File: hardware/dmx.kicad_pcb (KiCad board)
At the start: 4 copper layers, 70 x 70 mm, 63 parts, among them J101 CORTEX-DEBUG, J102 JAE_DX07S016JA3, J201 SJ2-25404B-SMT-TR, J301 SJ2-25404B-SMT-TR, SW101 SW_Push, SW102 SW_Push, U101 TPS78433QWDRBRQ1, U102 ATSAMD51G, U201 THVD24x2, U301 TLP2361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

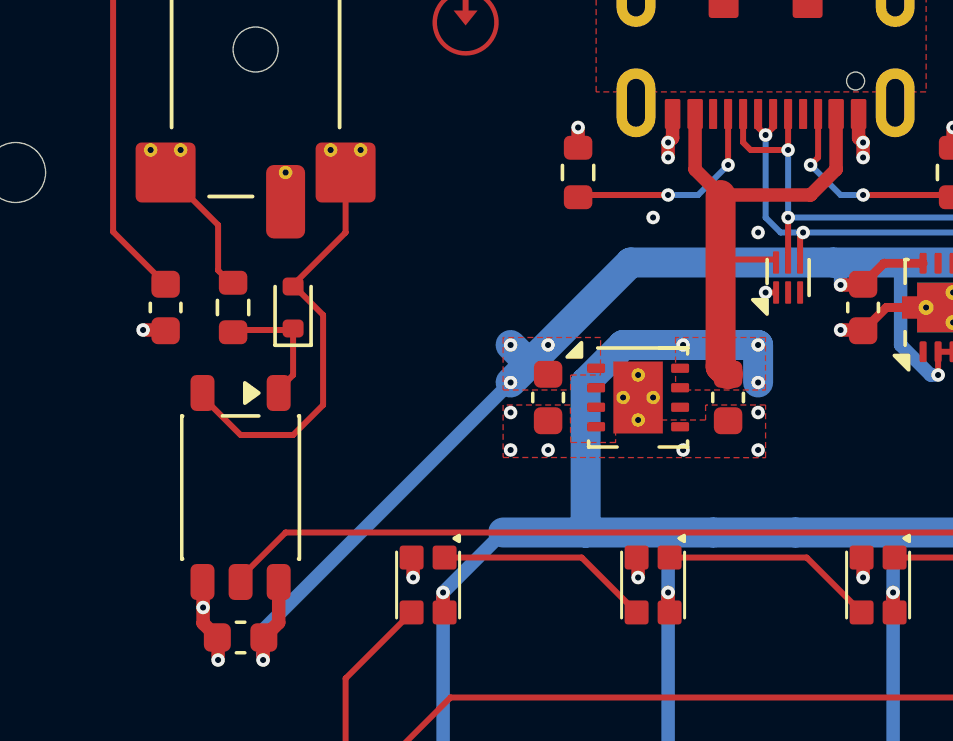
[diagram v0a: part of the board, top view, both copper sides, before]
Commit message: Update symbols
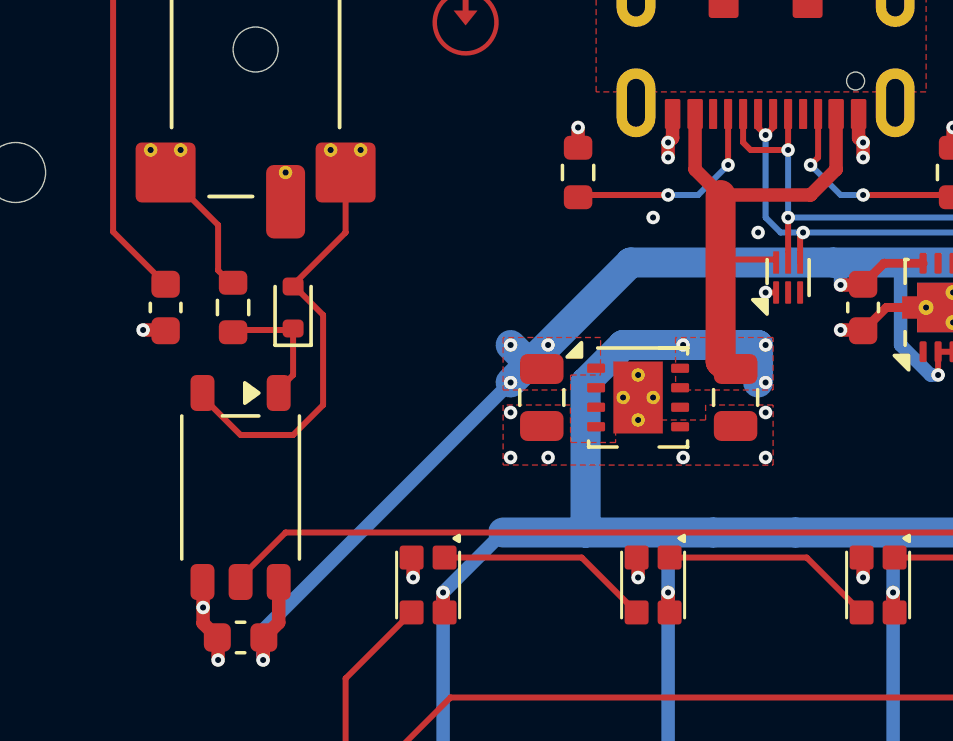
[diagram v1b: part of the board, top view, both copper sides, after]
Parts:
- C101, C102, C103, C104, C105, C108, C109, C201, C301, C302: footprint Capacitor_SMD:C_0603_1608Metric -> V2_Capacitor_SMD:C_0603
- C106, C107: footprint Capacitor_SMD:C_0603_1608Metric -> V2_Capacitor_SMD:C_0805
- D103: footprint LED_SMD:LED_0603_1608Metric -> V2_LED:LED_0603
- D301: footprint Diode_SMD:D_SOD-523 -> V2_Diode_SMD:D_SOD-523
- R101, R102, R103, R104, R301: footprint Resistor_SMD:R_0603_1608Metric -> V2_Resistor_SMD:R_0603
- U201: value THVD24x2 -> THVD2442
- U301: footprint Package_SO:SO-5-6_4.55x3.7mm_P1.27mm -> V2_Package_SO:SO-5-6_4.55x3.7mm_P1.27mm
- moved C106 0.25 mm to (151.0, 62.5)
- moved C107 0.21 mm to (144.5, 62.5)
- renumbered H103 to H102, H102 to H103, ICON102 to ICON101, ICON103 to ICON102, ICON101 to ICON103
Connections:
- net /LED-onboard renamed /LED-Board

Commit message: Refresh
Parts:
- C106, C107: footprint V2_Capacitor_SMD:C_0805 -> V2_Capacitor_SMD:C_0603
- FID101, FID102, FID103: value Fiducial -> Fiducial_Paste
- INFO102: value ORDER-NUMBER -> Order_Number
- J101: value CORTEX-DEBUG -> Cortex_Debug
- J102: value JAE_DX07S016JA3 -> DX07S016JA3
- SW101, SW102: value SW_Push -> SKSG
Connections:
- net USB-Shield renamed Earth

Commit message: Update power symbols
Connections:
- net Earth renamed Shield
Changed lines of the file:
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@@
 	(net 57 "/DMX Out/Ring")
 	(net 58 "/DMX Out/Tip")
-	(net 59 "Earth")
+	(net 59 "Shield")
 	(net 60 "/MIDI In/Ring")
 	(net 61 "/MIDI-In")
@@
 	(net 81 "unconnected-(J301-SW-Pad10)")
 	(net 82 "unconnected-(J201-SW-Pad10)")
-	(net 83 "unconnected-(J201-R2-Pad4)_2")
-	(net 84 "unconnected-(J301-R2-Pad4)_1")
+	(net 83 "unconnected-(J301-R2-Pad4)_1")
+	(net 84 "unconnected-(J201-R2-Pad4)_1")
 	(net 85 "unconnected-(J201-R2-Pad4)")
 	(net 86 "unconnected-(J201-SW-Pad10)_1")
-	(net 87 "unconnected-(J201-R2-Pad4)_1")
-	(net 88 "unconnected-(J301-R2-Pad4)")
-	(net 89 "unconnected-(J301-R2-Pad4)_2")
-	(net 90 "unconnected-(J301-SW-Pad10)_1")
+	(net 87 "unconnected-(J201-R2-Pad4)_2")
+	(net 88 "unconnected-(J301-SW-Pad10)_1")
+	(net 89 "unconnected-(J301-R2-Pad4)")
+	(net 90 "unconnected-(J301-R2-Pad4)_2")
 	(footprint "V2_Resistor_SMD:R_0603"
 		(layer "F.Cu")
@@
 			(keep_end_layers yes)
 			(zone_layer_connections)
-			(net 59 "Earth")
+			(net 59 "Shield")
 			(pinfunction "SHIELD")
 			(pintype "passive")
@@
 			(keep_end_layers yes)
 			(zone_layer_connections)
-			(net 59 "Earth")
+			(net 59 "Shield")
 			(pinfunction "SHIELD")
 			(pintype "passive")
@@
 			(layers "F.Cu" "F.Mask" "F.Paste")
 			(roundrect_rratio 0.1)
-			(net 59 "Earth")
+			(net 59 "Shield")
 			(pinfunction "SHIELD")
 			(pintype "passive")
@@
 			(layers "F.Cu" "F.Mask" "F.Paste")
 			(roundrect_rratio 0.1)
-			(net 59 "Earth")
+			(net 59 "Shield")
 			(pinfunction "SHIELD")
 			(pintype "passive")
@@
 			(keep_end_layers yes)
 			(zone_layer_connections)
-			(net 59 "Earth")
+			(net 59 "Shield")
 			(pinfunction "SHIELD")
 			(pintype "passive")
@@
 			(keep_end_layers yes)
 			(zone_layer_connections)
-			(net 59 "Earth")
+			(net 59 "Shield")
 			(pinfunction "SHIELD")
 			(pintype "passive")
@@
 			(keep_end_layers yes)
 			(zone_layer_connections)
-			(net 87 "unconnected-(J201-R2-Pad4)_1")
+			(net 87 "unconnected-(J201-R2-Pad4)_2")
 			(pinfunction "R2")
 			(pintype "passive+no_connect")
@@
 			(layers "F.Cu")
 			(roundrect_rratio 0.1)
-			(net 83 "unconnected-(J201-R2-Pad4)_2")
+			(net 84 "unconnected-(J201-R2-Pad4)_1")
 			(pinfunction "R2")
 			(pintype "passive+no_connect")
@@
 			)
 		)
+		(property "Rating" "25V"
+			(at 0 0 270)
+			(unlocked yes)
+			(layer "F.Fab")
+			(hide yes)
+			(effects
+				(font
+					(size 1 1)
+					(thickness 0.15)
+				)
+			)
+		)
 		(property ki_fp_filters "C_*")
 		(sheetname "/")
@@
 		)
 		(group ""
-			(members "404a20e9-3d3d-48ea-8a2c-ffcc6eda0b0e" "538f1783-69f6-4f90-927f-1181f1133400"
-				"afcb775d-0ac6-4813-9732-3cccbdd9df64" "e9cb6e1c-0535-4a7c-be3e-071c04aff0d2"
+			(members "19d6e09a-8b18-42a4-a25b-f7c27ec4f768" "3de2b706-0b65-4ad1-934f-0c5466142688"
+				"6d58372b-99b1-40f4-8215-0cc40e235ab4" "a6f77d4c-b74f-48b4-9c75-441ada7bb937"
 			)
 		)
 		(group ""
-			(members "2ae42719-b08b-49ad-8f29-a7ddc5eb57a1" "356651cd-24a7-4a63-8bf6-6a4ae89a0a40"
-				"9a1df374-816a-436a-b0db-4145c3be9c32" "a5fb0b80-161b-43ee-ba17-5dd0f0572550"
+			(members "07868cd9-0212-4992-b519-160e99a841ed" "2f61d476-e863-45ec-9c8c-8c44dc4076d2"
+				"8f538fec-782e-444f-a11c-de49b8ca3c26" "a942e51b-a22a-4f33-bdde-251ee4ea4f37"
 			)
 		)
@@
 			(keep_end_layers yes)
 			(zone_layer_connections)
-			(net 84 "unconnected-(J301-R2-Pad4)_1")
+			(net 83 "unconnected-(J301-R2-Pad4)_1")
 			(pinfunction "R2")
 			(pintype "passive+no_connect")
@@
 			(keep_end_layers yes)
 			(zone_layer_connections)
-			(net 89 "unconnected-(J301-R2-Pad4)_2")
+			(net 90 "unconnected-(J301-R2-Pad4)_2")
 			(pinfunction "R2")
 			(pintype "passive+no_connect")
@@
 			(layers "F.Cu")
 			(roundrect_rratio 0.1)
-			(net 88 "unconnected-(J301-R2-Pad4)")
+			(net 89 "unconnected-(J301-R2-Pad4)")
 			(pinfunction "R2")
 			(pintype "passive+no_connect")
@@
 			(layers "F.Cu")
 			(roundrect_rratio 0.2)
-			(net 90 "unconnected-(J301-SW-Pad10)_1")
+			(net 88 "unconnected-(J301-SW-Pad10)_1")
 			(pinfunction "SW")
 			(pintype "passive+no_connect")
@@
 			)
 		)
+		(property "Rating" "25V"
+			(at 0 0 270)
+			(unlocked yes)
+			(layer "F.Fab")
+			(hide yes)
+			(effects
+				(font
+					(size 1 1)
+					(thickness 0.15)
+				)
+			)
+		)
 		(property ki_fp_filters "C_*")
 		(sheetname "/")
@@
 	(zone
 		(net 59)
-		(net_name "Earth")
+		(net_name "Shield")
 		(layer "F.Cu")
 		(hatch edge 0.508)

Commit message: Update parts
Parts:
- C106, C107: footprint V2_Capacitor_SMD:C_0603 -> V2_Capacitor_SMD:C_0805
